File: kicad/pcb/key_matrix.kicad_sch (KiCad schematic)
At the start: 73 parts, among them SW1 SW_Push, SW10 SW_Push, SW11 SW_Push, SW12 SW_Push, SW13 SW_Push, SW14 SW_Push, SW15 SW_Push, SW16 SW_Push, SW17 SW_Push, SW18 SW_Push, SW19 SW_Push, SW2 SW_Push, SW20 SW_Push, SW21 SW_Push, SW22 SW_Push, SW23 SW_Push, SW24 SW_Push, SW25 SW_Push, SW26 SW_Push, SW27 SW_Push, SW28 SW_Push, SW29 SW_Push, SW3 SW_Push, SW30 SW_Push, SW31 SW_Push, SW32 SW_Push, SW33 SW_Push, SW34 SW_Push, SW35 SW_Push, SW36 Rotary_Encoder_Switch, SW4 SW_Push, SW5 SW_Push, SW6 SW_Push, SW7 SW_Push, SW8 SW_Push, SW9 SW_Push

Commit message: v0.2.2
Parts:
- SW36: footprint modified_footrprints:RotaryEncoder_EC11_no_mp -> modified_footprints:RotaryEncoder_EC11_no_mp
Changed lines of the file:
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@@
       (effects (font (size 1.27 1.27)))
     )
-    (property "Footprint" "modified_footrprints:RotaryEncoder_EC11_no_mp" (at 93.345 159.639 0)
+    (property "Footprint" "modified_footprints:RotaryEncoder_EC11_no_mp" (at 93.345 159.639 0)
       (effects (font (size 1.27 1.27)) hide)
     )

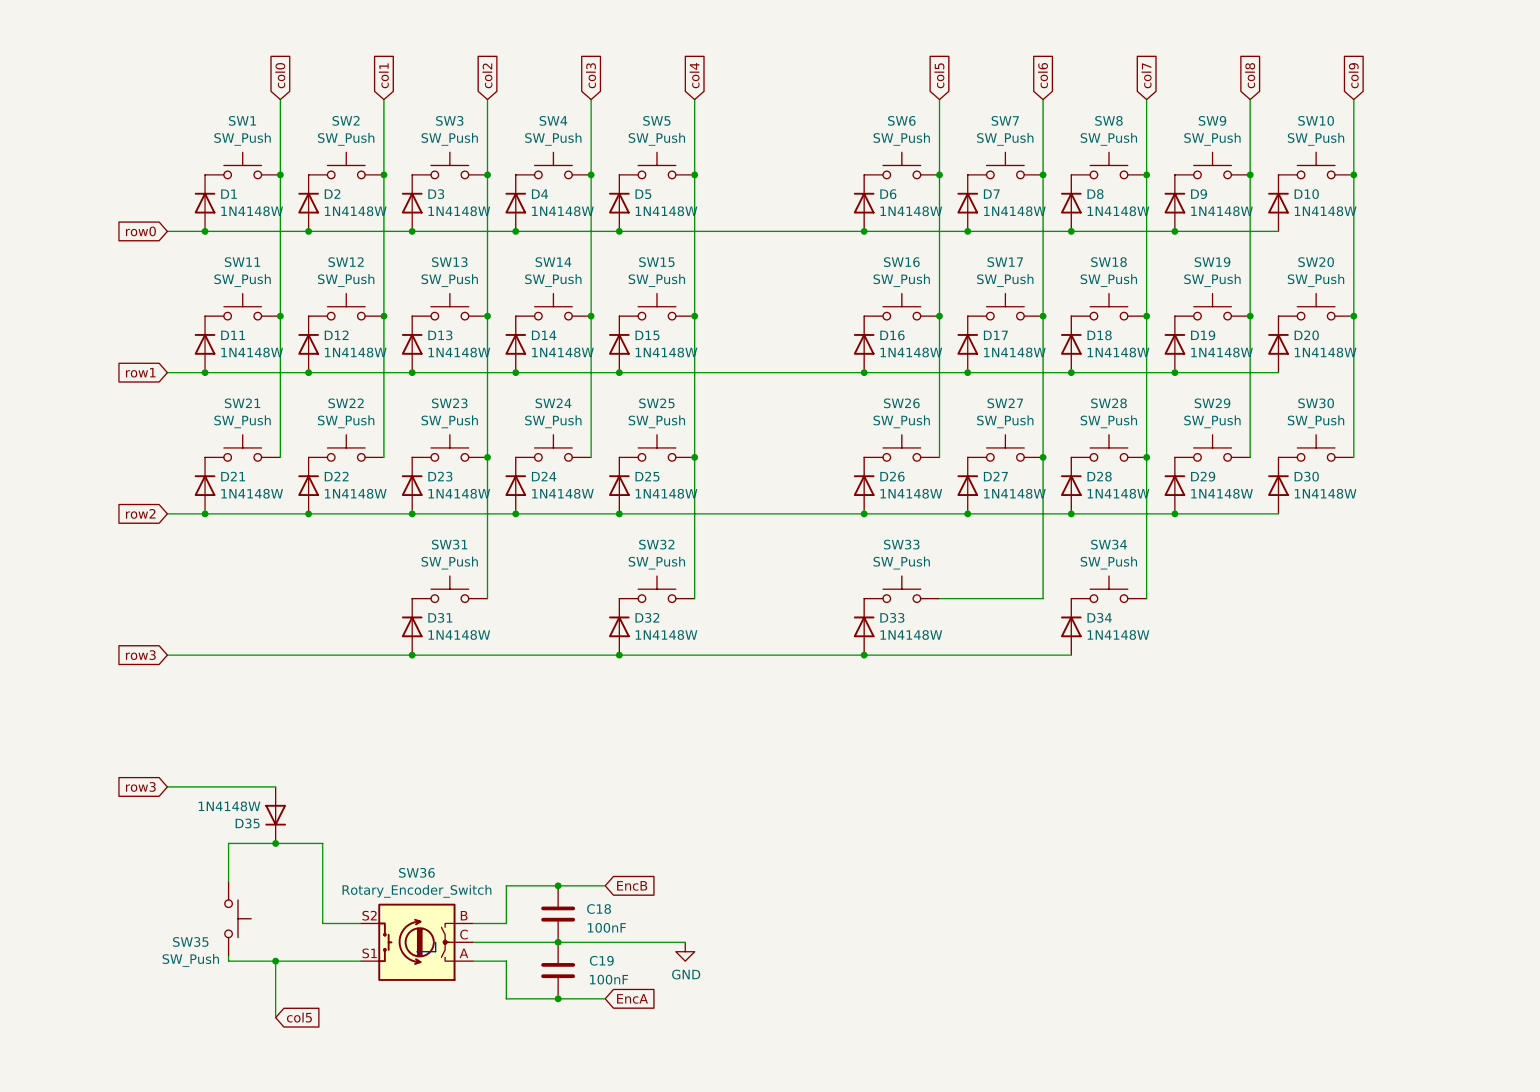
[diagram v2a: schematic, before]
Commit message: Initial SAM/nRF52 version.
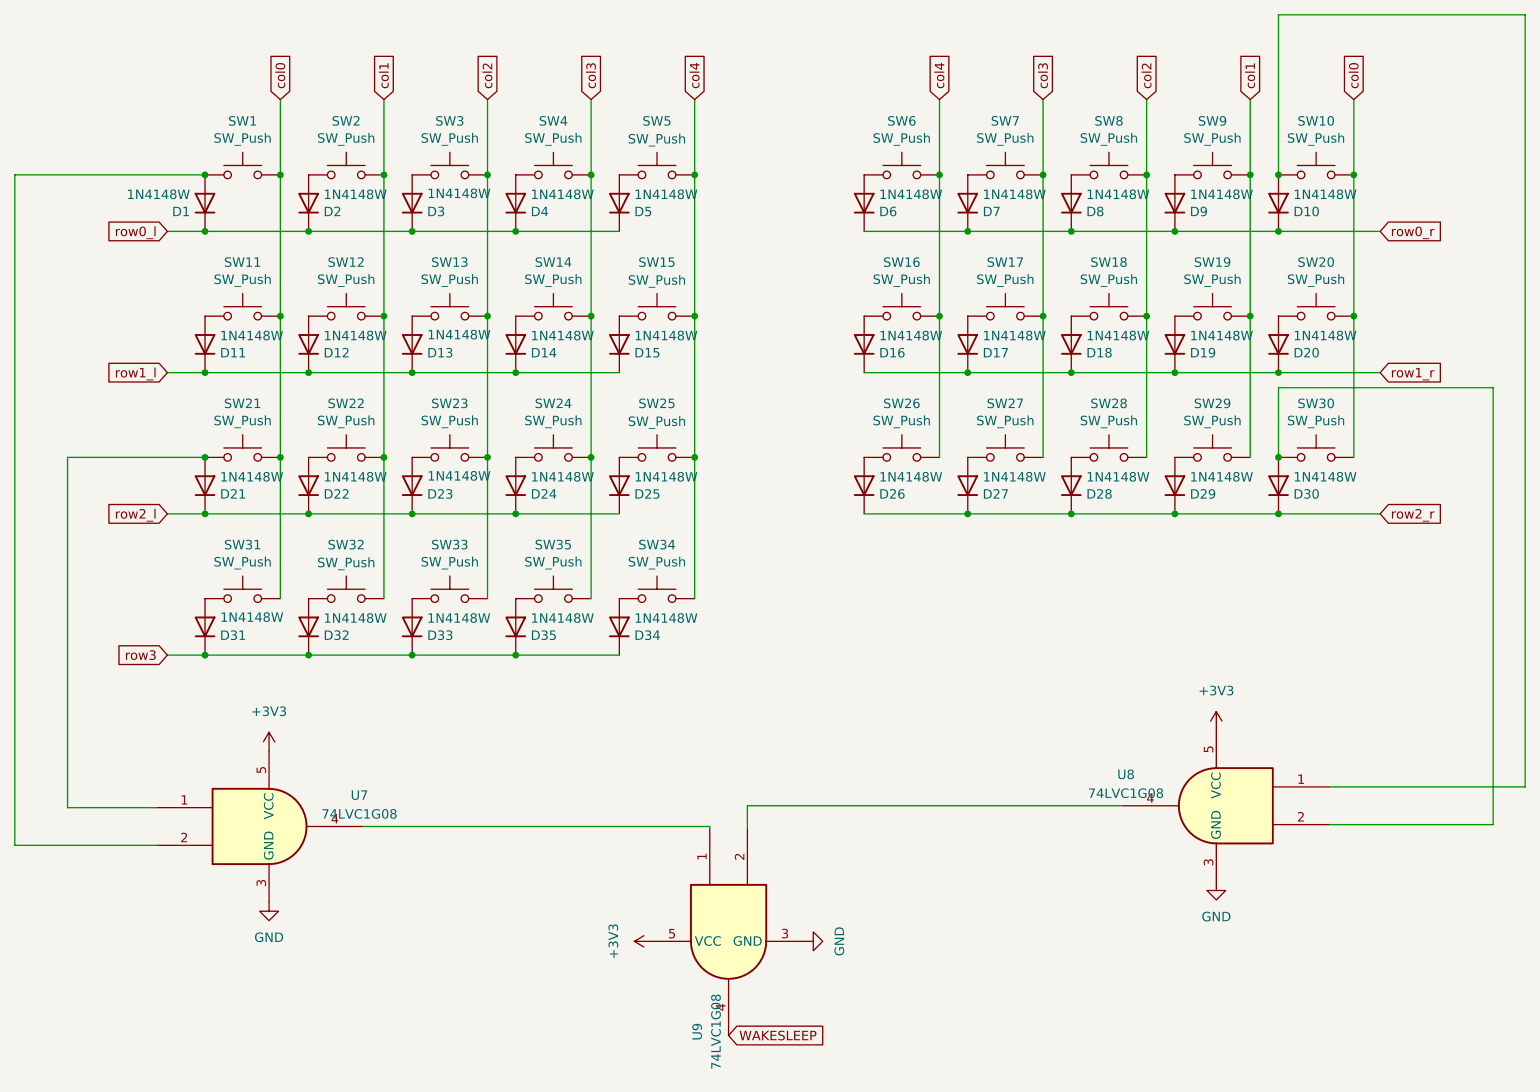
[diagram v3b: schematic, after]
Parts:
- removed C18, C19: 100nF, Capacitor_SMD:C_0402_1005Metric, symbol Device:C
- removed D35: 1N4148W, Diode_SMD:D_SOD-123, symbol Diode:1N4148
- removed SW35: SW_Push, MX_Alps_Hybrid:MX-Alps-Hybrid-1U, symbol Switch:SW_Push
- removed SW36: Rotary_Encoder_Switch, modified_footprints:RotaryEncoder_EC11_no_mp, symbol LeChiffre-rescue:Rotary_Encoder_Switch-Device
- added D34: 1N4148W, Diode_SMD:D_SOD-123, symbol Diode:1N4148
- added SW34: SW_Push, MX_hotswap_alps:MX-Hotswap-Alps-1.25U, symbol Switch:SW_Push
- added U7, U8, U9: 74LVC1G08, Package_TO_SOT_SMD:SOT-23-5_HandSoldering, symbol 74xGxx:74LVC1G08
- SW33: footprint MX_hotswap_alps:MX-Hotswap-Alps-2U -> MX_hotswap_alps:MX-Hotswap-Alps-1U
- SW35: renamed from SW34; footprint MX_hotswap_alps:MX-Hotswap-Alps-1.25U -> MX_hotswap_alps:MX-Hotswap-Alps-2U
- renumbered D34 to D35
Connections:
- net col5 is gone; now on net col4: SW16.2, SW26.2, SW6.2
- net col8 is gone; now on net col1: SW19.2, SW29.2, SW9.2
- net col9 is gone; now on net col0: SW10.2, SW20.2, SW30.2
- net GND: now also U7.3 (GND), U8.3 (GND), U9.3 (GND)
- net col0: now also SW31.2
- net col1: now also SW32.2
- net col2: now also SW18.2, SW28.2, SW33.2, SW8.2; no longer SW31.2
- net col3: now also SW17.2, SW27.2, SW35.2, SW7.2
- net col4: now also SW34.2; no longer SW32.2
- net row3: now also D31.1 (K), D32.1 (K), D33.1 (K), D35.1 (K), D34.1 (K); no longer D31.2 (A), D32.2 (A), D33.2 (A), D35.2 (A)
- net at SW20.1: now also D20.2 (A); no longer D20.1 (K)
- net at SW14.1: now also D14.2 (A); no longer D14.1 (K)
- net at SW35.1: now also D35.2 (A); no longer D35.1 (K)
- net at SW22.1: now also D22.2 (A); no longer D22.1 (K)
- net at SW5.1: now also D5.2 (A); no longer D5.1 (K)
- net at SW23.1: now also D23.2 (A); no longer D23.1 (K)
- net at SW12.1: now also D12.2 (A); no longer D12.1 (K)
- net at SW19.1: now also D19.2 (A); no longer D19.1 (K)
- net at SW15.1: now also D15.2 (A); no longer D15.1 (K)
- net at SW28.1: now also D28.2 (A); no longer D28.1 (K)
- net at SW33.1: now also D33.2 (A); no longer D33.1 (K)
- net at SW18.1: now also D18.2 (A); no longer D18.1 (K)
- net at SW27.1: now also D27.2 (A); no longer D27.1 (K)
- net at SW10.1: now also D10.2 (A), U8.1; no longer D10.1 (K)
- net at SW26.1: now also D26.2 (A); no longer D26.1 (K)
- net at SW13.1: now also D13.2 (A); no longer D13.1 (K)
- net at SW24.1: now also D24.2 (A); no longer D24.1 (K)
- net at SW1.1: now also D1.2 (A), U7.2; no longer D1.1 (K)
- net at SW2.1: now also D2.2 (A); no longer D2.1 (K)
- net at SW29.1: now also D29.2 (A); no longer D29.1 (K)
- net at SW16.1: now also D16.2 (A); no longer D16.1 (K)
- net at SW7.1: now also D7.2 (A); no longer D7.1 (K)
- net at SW32.1: now also D32.2 (A); no longer D32.1 (K)
- net at SW6.1: now also D6.2 (A); no longer D6.1 (K)
- net at SW11.1: now also D11.2 (A); no longer D11.1 (K)
- net at SW17.1: now also D17.2 (A); no longer D17.1 (K)
- net at SW3.1: now also D3.2 (A); no longer D3.1 (K)
- net at SW31.1: now also D31.2 (A); no longer D31.1 (K)
- net at SW4.1: now also D4.2 (A); no longer D4.1 (K)
- net at SW30.1: now also D30.2 (A), U8.2; no longer D30.1 (K)
- net at SW9.1: now also D9.2 (A); no longer D9.1 (K)
- net at SW8.1: now also D8.2 (A); no longer D8.1 (K)
- net at SW21.1: now also D21.2 (A), U7.1; no longer D21.1 (K)
- net at SW25.1: now also D25.2 (A); no longer D25.1 (K)
- removed net col6: SW17.2, SW27.2, SW33.2, SW7.2
- removed net col7: SW18.2, SW28.2, SW35.2, SW8.2
- removed net row0: D1.2 (A), D10.2 (A), D2.2 (A), D3.2 (A), D4.2 (A), D5.2 (A), D6.2 (A), D7.2 (A), D8.2 (A), D9.2 (A)
- removed net row1: D11.2 (A), D12.2 (A), D13.2 (A), D14.2 (A), D15.2 (A), D16.2 (A), D17.2 (A), D18.2 (A), D19.2 (A), D20.2 (A)
- removed net row2: D21.2 (A), D22.2 (A), D23.2 (A), D24.2 (A), D25.2 (A), D26.2 (A), D27.2 (A), D28.2 (A), D29.2 (A), D30.2 (A)
- new net: U7.4, U9.1
- new net: D34.2 (A), SW34.1
- new net: U8.4, U9.2
- new net +3V3: U7.5 (VCC), U8.5 (VCC), U9.5 (VCC)
- new net WAKESLEEP: U9.4
- new net row0_l: D1.1 (K), D2.1 (K), D3.1 (K), D4.1 (K), D5.1 (K)
- new net row0_r: D10.1 (K), D6.1 (K), D7.1 (K), D8.1 (K), D9.1 (K)
- new net row1_l: D11.1 (K), D12.1 (K), D13.1 (K), D14.1 (K), D15.1 (K)
- new net row1_r: D16.1 (K), D17.1 (K), D18.1 (K), D19.1 (K), D20.1 (K)
- new net row2_l: D21.1 (K), D22.1 (K), D23.1 (K), D24.1 (K), D25.1 (K)
- new net row2_r: D26.1 (K), D27.1 (K), D28.1 (K), D29.1 (K), D30.1 (K)
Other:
- moved on the sheet: D1, D31, D32, D33, D35, SW31, SW32, SW33, SW35
